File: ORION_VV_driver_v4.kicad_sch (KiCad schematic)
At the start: 146 parts, among them J11 Conn_01x02, J12 Conn_01x05, J13 Conn_01x05, J15 Conn_01x02, J2 Conn_01x04, J3 Conn_01x04, J4 Conn_01x06, J5 Conn_01x07, J6 Conn_01x07, Q1 IRF8721PBF-1, Q10 IRF8721PBF-1, Q11 IRF8721PBF-1, Q12 IRF8721PBF-1, Q2 IRF8721PBF-1, Q3 IRF8721PBF-1, Q4 IRF8721PBF-1, Q5 IRF8721PBF-1, Q6 IRF8721PBF-1, Q7 IRF8721PBF-1, Q8 IRF8721PBF-1, Q9 IRF8721PBF-1, SW1 SW_Push, SW2 SW_Push, SW3 SW_Push, SW4 SW_Push, SW5 SW_Push, U1 BD9G101G, U2 L78L33_SOT89, U3 MAX3051, U5 INA199, U6 INA199, Y1 Resonator

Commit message: 配線とシルクの改善
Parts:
- added C53, C54: 0.1u, Capacitor_SMD:C_0402_1005Metric, symbol Device:C
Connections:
- net 3V3_HARF_REF: now also C53.2, C54.2
- net GND: now also C53.1, C54.1
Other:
- moved on the sheet: C14, C15, C2, C23, C4, C46, C47, C48, C49, C5, D14, D15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

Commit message: 微調整
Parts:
- added J1, J10, J14, J7, J8, J9: Conn_01x01, TestPoint:TestPoint_Pad_D1.0mm, symbol Connector_Generic:Conn_01x01
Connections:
- net M0_UL: now also J1.1 (Pin_1)
- net M0_VL: now also J7.1 (Pin_1)
- net M0_WL: now also J8.1 (Pin_1)
- net M1_UL: now also J9.1 (Pin_1)
- net M1_VL: now also J10.1 (Pin_1)
- net M1_WL: now also J14.1 (Pin_1)
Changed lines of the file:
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@@
     (effects (font (size 1.27 1.27)) (justify right bottom))
   )
+  (label "M0_UL" (at 328.93 205.74 180)
+    (effects (font (size 1.27 1.27)) (justify right bottom))
+  )
   (label "M0_UH" (at 233.68 156.21 0)
     (effects (font (size 1.27 1.27)) (justify left bottom))
@@
     (effects (font (size 1.27 1.27)) (justify right bottom))
   )
+  (label "M0_VL" (at 328.93 210.82 180)
+    (effects (font (size 1.27 1.27)) (justify right bottom))
+  )
   (label "M0_W" (at 492.76 193.04 0)
     (effects (font (size 1.27 1.27)) (justify left bottom))
@@
     (effects (font (size 1.27 1.27)) (justify right bottom))
   )
+  (label "M1_VL" (at 328.93 240.03 180)
+    (effects (font (size 1.27 1.27)) (justify right bottom))
+  )
   (label "M1_UL" (at 330.2 298.45 180)
     (effects (font (size 1.27 1.27)) (justify right bottom))
@@
     (effects (font (size 1.27 1.27)) (justify right bottom))
   )
+  (label "M1_UL" (at 328.93 233.68 180)
+    (effects (font (size 1.27 1.27)) (justify right bottom))
+  )
   (label "CAN_L" (at 215.9 327.66 180)
     (effects (font (size 1.27 1.27)) (justify right bottom))
@@
     (effects (font (size 1.27 1.27)) (justify right bottom))
   )
+  (label "M0_WL" (at 328.93 215.9 180)
+    (effects (font (size 1.27 1.27)) (justify right bottom))
+  )
   (label "LED_0" (at 198.12 212.09 180)
     (effects (font (size 1.27 1.27)) (justify right bottom))
@@
     (effects (font (size 1.27 1.27)) (justify right bottom))
   )
+  (label "M1_WL" (at 328.93 246.38 180)
+    (effects (font (size 1.27 1.27)) (justify right bottom))
+  )
   (label "SW3" (at 198.12 186.69 180)
     (effects (font (size 1.27 1.27)) (justify right bottom))
@@
     (pin "2")
   )
+  (symbol (lib_id "Connector_Generic:Conn_01x01") (at 334.01 215.9 0) (unit 1)
+    (in_bom yes) (on_board yes) (fields_autoplaced)
+    (property "Reference" "J8" (id 0) (at 336.55 214.6299 0)
+      (effects (font (size 1.27 1.27)) (justify left))
+    )
+    (property "Value" "Conn_01x01" (id 1) (at 336.55 217.1699 0)
+      (effects (font (size 1.27 1.27)) (justify left))
+    )
+    (property "Footprint" "TestPoint:TestPoint_Pad_D1.0mm" (id 2) (at 334.01 215.9 0)
+      (effects (font (size 1.27 1.27)) hide)
+    )
+    (property "Datasheet" "~" (id 3) (at 334.01 215.9 0)
+      (effects (font (size 1.27 1.27)) hide)
+    )
+    (pin "1")
+  )
   (symbol (lib_id "Device:C") (at 516.89 326.39 0) (unit 1)
     (in_bom yes) (on_board yes)
@@
     (pin "2")
   )
+  (symbol (lib_id "Connector_Generic:Conn_01x01") (at 334.01 210.82 0) (unit 1)
+    (in_bom yes) (on_board yes) (fields_autoplaced)
+    (property "Reference" "J7" (id 0) (at 336.55 209.5499 0)
+      (effects (font (size 1.27 1.27)) (justify left))
+    )
+    (property "Value" "Conn_01x01" (id 1) (at 336.55 212.0899 0)
+      (effects (font (size 1.27 1.27)) (justify left))
+    )
+    (property "Footprint" "TestPoint:TestPoint_Pad_D1.0mm" (id 2) (at 334.01 210.82 0)
+      (effects (font (size 1.27 1.27)) hide)
+    )
+    (property "Datasheet" "~" (id 3) (at 334.01 210.82 0)
+      (effects (font (size 1.27 1.27)) hide)
+    )
+    (pin "1")
+  )
   (symbol (lib_id "power:GNDPWR") (at 496.57 256.54 0) (unit 1)
     (in_bom yes) (on_board yes) (fields_autoplaced)
@@
     (pin "2")
   )
+  (symbol (lib_id "Connector_Generic:Conn_01x01") (at 334.01 246.38 0) (unit 1)
+    (in_bom yes) (on_board yes) (fields_autoplaced)
+    (property "Reference" "J14" (id 0) (at 336.55 245.1099 0)
+      (effects (font (size 1.27 1.27)) (justify left))
+    )
+    (property "Value" "Conn_01x01" (id 1) (at 336.55 247.6499 0)
+      (effects (font (size 1.27 1.27)) (justify left))
+    )
+    (property "Footprint" "TestPoint:TestPoint_Pad_D1.0mm" (id 2) (at 334.01 246.38 0)
+      (effects (font (size 1.27 1.27)) hide)
+    )
+    (property "Datasheet" "~" (id 3) (at 334.01 246.38 0)
+      (effects (font (size 1.27 1.27)) hide)
+    )
+    (pin "1")
+  )
   (symbol (lib_id "Device:R") (at 425.45 350.52 90) (unit 1)
     (in_bom yes) (on_board yes) (fields_autoplaced)
@@
     (pin "2")
   )
+  (symbol (lib_id "Connector_Generic:Conn_01x01") (at 334.01 240.03 0) (unit 1)
+    (in_bom yes) (on_board yes) (fields_autoplaced)
+    (property "Reference" "J10" (id 0) (at 336.55 238.7599 0)
+      (effects (font (size 1.27 1.27)) (justify left))
+    )
+    (property "Value" "Conn_01x01" (id 1) (at 336.55 241.2999 0)
+      (effects (font (size 1.27 1.27)) (justify left))
+    )
+    (property "Footprint" "TestPoint:TestPoint_Pad_D1.0mm" (id 2) (at 334.01 240.03 0)
+      (effects (font (size 1.27 1.27)) hide)
+    )
+    (property "Datasheet" "~" (id 3) (at 334.01 240.03 0)
+      (effects (font (size 1.27 1.27)) hide)
+    )
+    (pin "1")
+  )
   (symbol (lib_id "Device:C") (at 474.98 97.79 180) (unit 1)
     (in_bom yes) (on_board yes) (fields_autoplaced)
@@
     (pin "2")
   )
+  (symbol (lib_id "Connector_Generic:Conn_01x01") (at 334.01 233.68 0) (unit 1)
+    (in_bom yes) (on_board yes) (fields_autoplaced)
+    (property "Reference" "J9" (id 0) (at 336.55 232.4099 0)
+      (effects (font (size 1.27 1.27)) (justify left))
+    )
+    (property "Value" "Conn_01x01" (id 1) (at 336.55 234.9499 0)
+      (effects (font (size 1.27 1.27)) (justify left))
+    )
+    (property "Footprint" "TestPoint:TestPoint_Pad_D1.0mm" (id 2) (at 334.01 233.68 0)
+      (effects (font (size 1.27 1.27)) hide)
+    )
+    (property "Datasheet" "~" (id 3) (at 334.01 233.68 0)
+      (effects (font (size 1.27 1.27)) hide)
+    )
+    (pin "1")
+  )
   (symbol (lib_id "power:+3.3V") (at 340.36 34.29 0) (unit 1)
     (in_bom yes) (on_board yes) (fields_autoplaced)
@@
     (pin "8")
   )
+  (symbol (lib_id "Connector_Generic:Conn_01x01") (at 334.01 205.74 0) (unit 1)
+    (in_bom yes) (on_board yes) (fields_autoplaced)
+    (property "Reference" "J1" (id 0) (at 336.55 204.4699 0)
+      (effects (font (size 1.27 1.27)) (justify left))
+    )
+    (property "Value" "Conn_01x01" (id 1) (at 336.55 207.0099 0)
+      (effects (font (size 1.27 1.27)) (justify left))
+    )
+    (property "Footprint" "TestPoint:TestPoint_Pad_D1.0mm" (id 2) (at 334.01 205.74 0)
+      (effects (font (size 1.27 1.27)) hide)
+    )
+    (property "Datasheet" "~" (id 3) (at 334.01 205.74 0)
+      (effects (font (size 1.27 1.27)) hide)
+    )
+    (pin "1")
+  )
   (symbol (lib_id "power:+9V") (at 92.71 262.89 0) (unit 1)
     (in_bom yes) (on_board yes) (fields_autoplaced)
@@
       (reference "GD2") (unit 1) (value "FD6288Q") (footprint "Package_DFN_QFN:HVQFN-24-1EP_4x4mm_P0.5mm_EP2.6x2.6mm_ThermalVias")
     )
+    (path "/e27d1833-79bc-4066-95bb-751897c3f062"
+      (reference "J1") (unit 1) (value "Conn_01x01") (footprint "TestPoint:TestPoint_Pad_D1.0mm")
+    )
     (path "/a07447f9-d167-4664-b5e4-c41c1ec453be"
       (reference "J2") (unit 1) (value "Conn_01x04") (footprint "Connector_Hirose:Hirose_DF13-04P-1.25DSA_1x04_P1.25mm_Vertical")
@@
       (reference "J6") (unit 1) (value "Conn_01x07") (footprint "Connector_Hirose:Hirose_DF13-07P-1.25DSA_1x07_P1.25mm_Vertical")
     )
+    (path "/08b44f28-5e79-478e-a7d2-83abf1f1e29d"
+      (reference "J7") (unit 1) (value "Conn_01x01") (footprint "TestPoint:TestPoint_Pad_D1.0mm")
+    )
+    (path "/08333a5e-8c4c-4b14-ad07-94ddb3a9af9b"
+      (reference "J8") (unit 1) (value "Conn_01x01") (footprint "TestPoint:TestPoint_Pad_D1.0mm")
+    )
+    (path "/8a5601a2-4fdf-4bc8-ba05-f12e2321d019"
+      (reference "J9") (unit 1) (value "Conn_01x01") (footprint "TestPoint:TestPoint_Pad_D1.0mm")
+    )
+    (path "/7afcac36-27f0-464c-ab02-1219eeec16fa"
+      (reference "J10") (unit 1) (value "Conn_01x01") (footprint "TestPoint:TestPoint_Pad_D1.0mm")
+    )
     (path "/fb307618-0df6-4f43-aeb7-1a7b6e15712f"
       (reference "J11") (unit 1) (value "Conn_01x02") (footprint "Connector_AMASS:AMASS_XT30PW-M_1x02_P2.50mm_Horizontal")
@@
       (reference "J13") (unit 1) (value "Conn_01x05") (footprint "user:2053380003")
     )
+    (path "/6bb49902-ad3d-4400-914a-f458f6fd6ea3"
+      (reference "J14") (unit 1) (value "Conn_01x01") (footprint "TestPoint:TestPoint_Pad_D1.0mm")
+    )
     (path "/49866eaa-1518-4369-84de-63f174cd5f42"

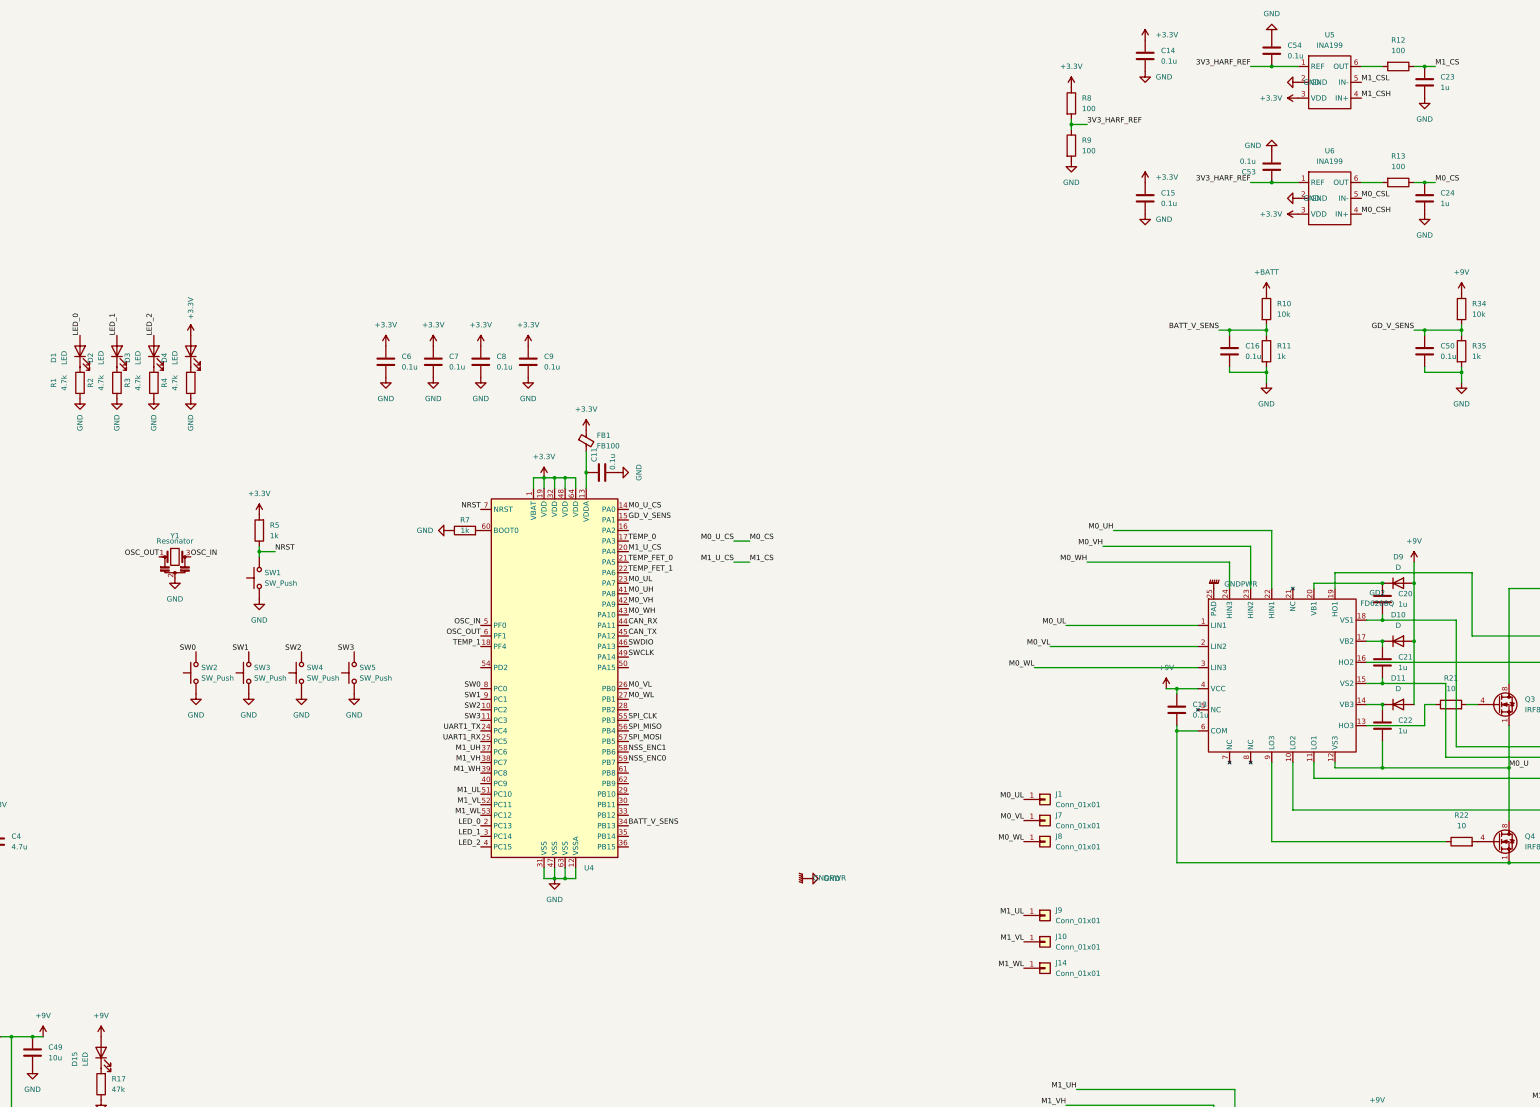
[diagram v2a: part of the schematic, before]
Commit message: シルク追加
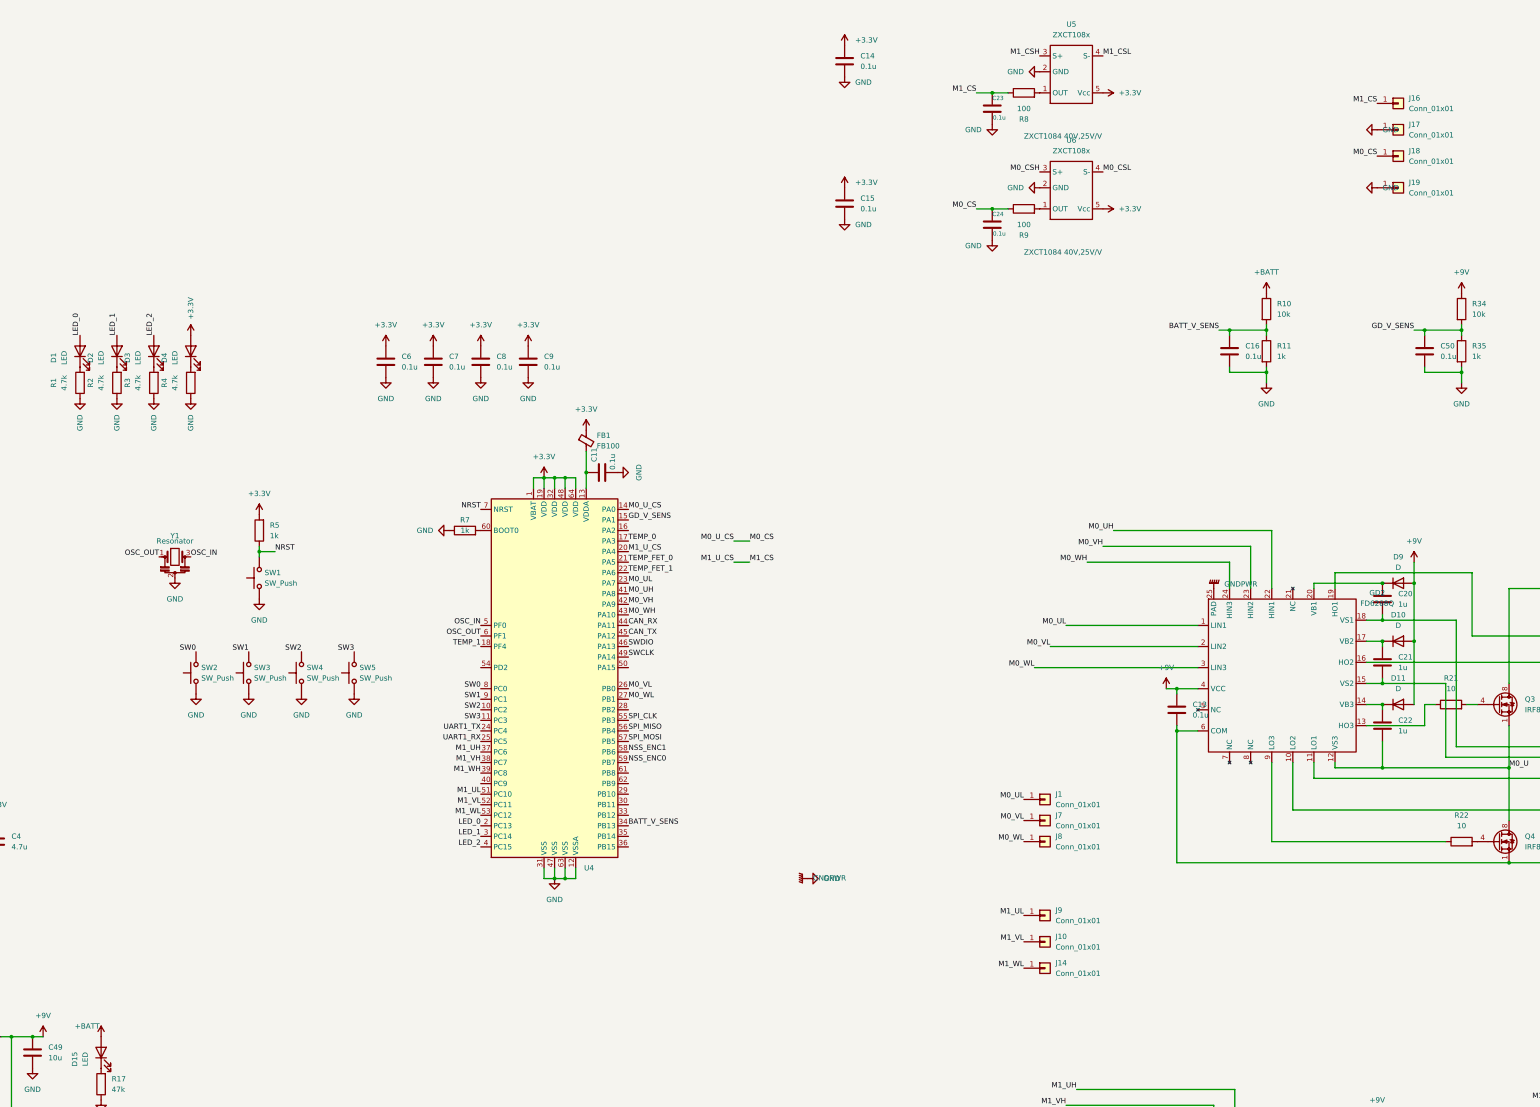
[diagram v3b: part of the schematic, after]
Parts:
- removed C23, C24: 1u, Capacitor_SMD:C_0603_1608Metric, symbol Device:C
- removed C53, C54: 0.1u, Capacitor_SMD:C_0402_1005Metric, symbol Device:C
- removed R12, R13: 100, Resistor_SMD:R_0603_1608Metric, symbol Device:R
- removed U5, U6: INA199, Package_TO_SOT_SMD:SOT-363_SC-70-6, symbol User:INA199
- added C23, C24: 0.1u, Capacitor_SMD:C_0603_1608Metric, symbol SSL_BST_ver1.3-rescue:C
- added J16, J17, J18, J19: Conn_01x01, TestPoint:TestPoint_Loop_D2.60mm_Drill0.9mm_Beaded, symbol Connector_Generic:Conn_01x01
- added U5, U6: ZXCT108x, Package_TO_SOT_SMD:SOT-23-5, symbol User:ZXCT108x
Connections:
- net +3V3: now also U5.5 (Vcc), U6.5 (Vcc); no longer R8.1
- net +9V: no longer D15.2 (A)
- net +BATT: now also D15.2 (A), U5.3 (S+), U6.3 (S+)
- net GND: now also C23.2, C24.2, J17.1 (Pin_1), J19.1 (Pin_1), U5.2 (GND), U6.2 (GND); no longer R9.2
- net M0_CS: now also R9.1, C24.1, J18.1 (Pin_1)
- net M0_CSL: now also U6.4 (S-)
- net M1_CS: now also R8.1, C23.1, J16.1 (Pin_1)
- net M1_CSL: now also U5.4 (S-)
- net 3V3_HARF_REF: no longer names the net of R8.2
- net 3V3_HARF_REF: now also U5.1 (OUT); no longer R9.1
- new net: R9.2, U6.1 (OUT)
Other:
- note added: "ZXCT1084 40V,25V/V"
- moved on the sheet: C14, C15
